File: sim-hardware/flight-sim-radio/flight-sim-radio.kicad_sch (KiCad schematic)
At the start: 22 parts, among them J1 Conn_01x04, J2 Conn_01x03, J3 Conn_01x08, SW1 SW_Push, SW2 SW_Rotary_1x7_MP, SW3 RotaryEncoder_Switch, SW4 RotaryEncoder_Switch, U1 74LS148, U4 TM1637, U5 TM1637

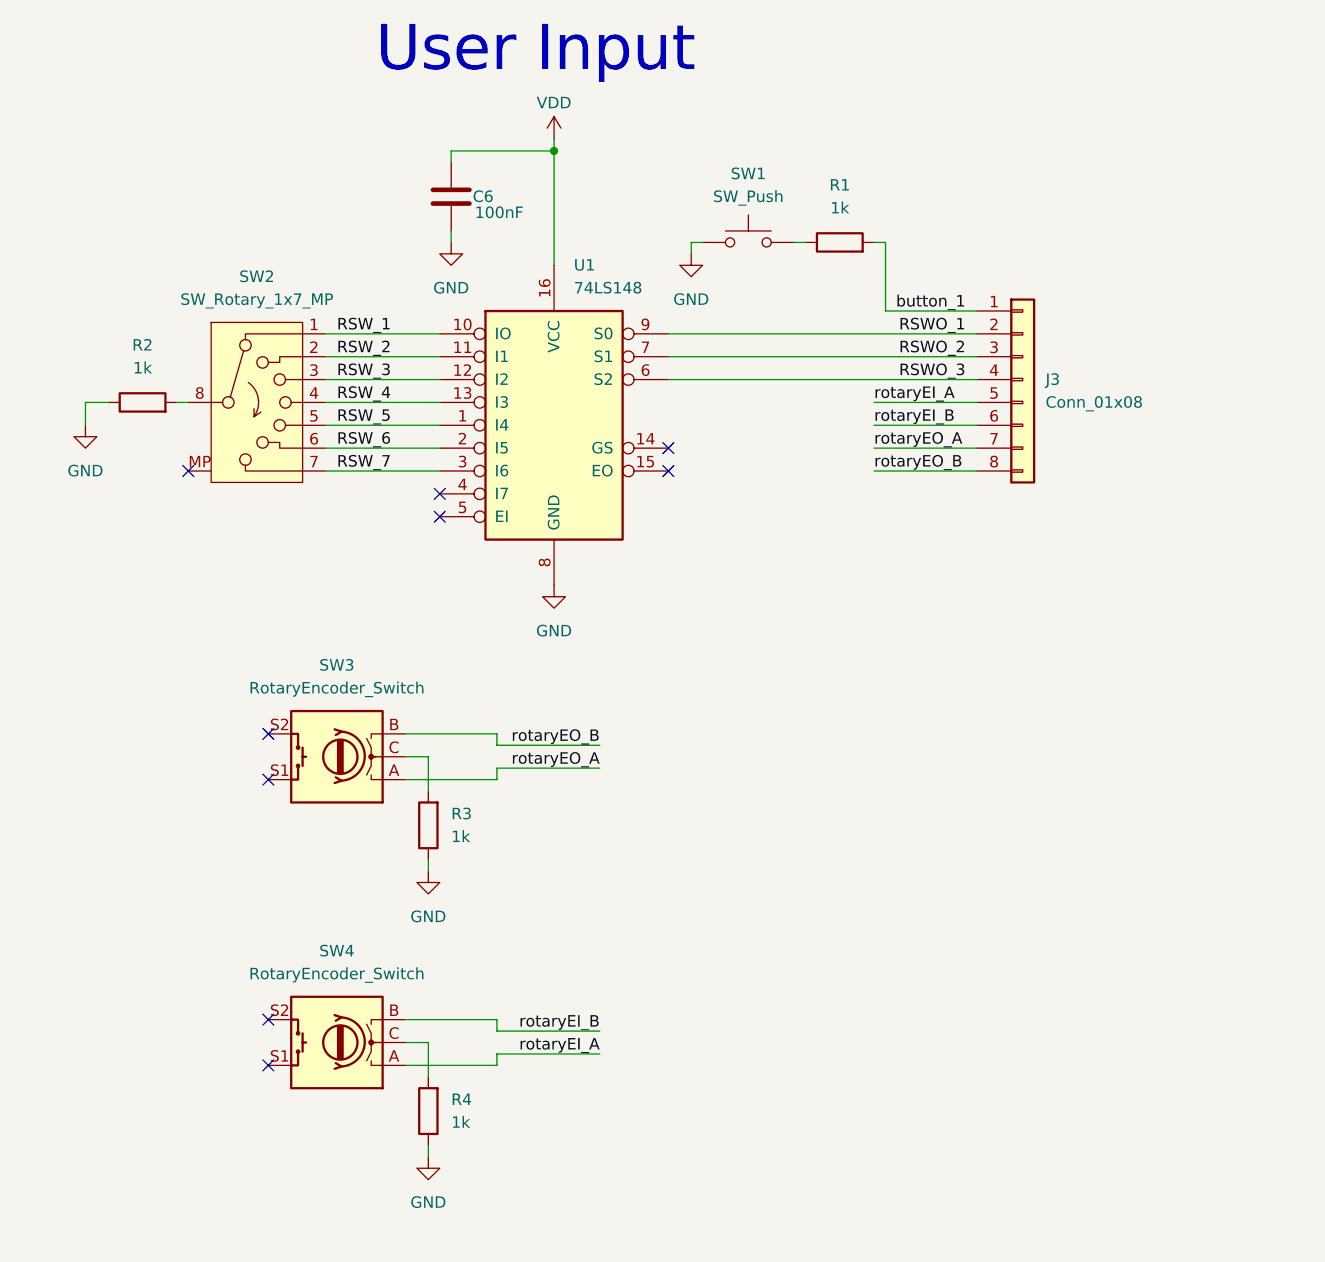
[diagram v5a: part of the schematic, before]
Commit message: input layed out
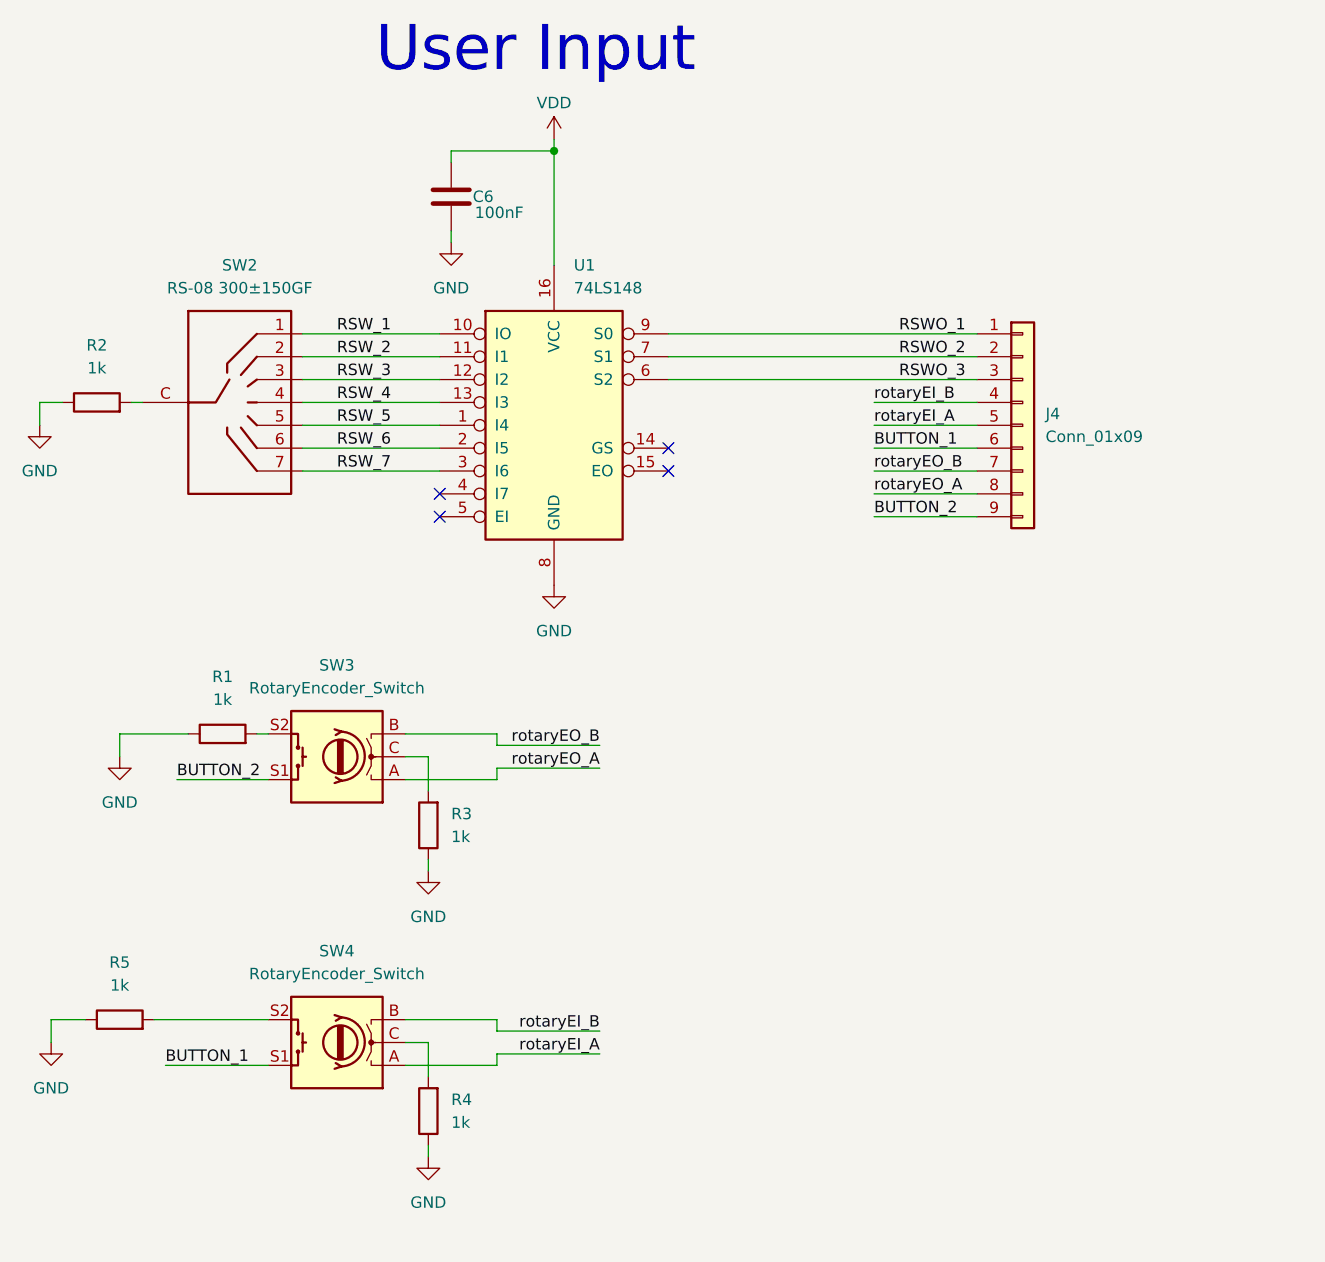
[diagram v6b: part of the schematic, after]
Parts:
- removed J3: Conn_01x08, Connector_PinHeader_2.54mm:PinHeader_1x08_P2.54mm_Vertical, symbol Connector_Generic:Conn_01x08
- removed SW1: SW_Push, Button_Switch_THT:SW_PUSH-12mm, symbol Switch:SW_Push
- removed SW2: SW_Rotary_1x7_MP, Connector_PinHeader_2.54mm:PinHeader_1x09_P2.54mm_Vertical, symbol Switch:SW_Rotary_1x7_MP
- added J4: Conn_01x09, Connector_PinHeader_2.54mm:PinHeader_1x09_P2.54mm_Vertical, symbol Connector_Generic:Conn_01x09
- added R5: 1k, Resistor_THT:R_Axial_DIN0414_L11.9mm_D4.5mm_P15.24mm_Horizontal, symbol Device:R
- added SW2: RS-08 300±150GF, radio_footprints:SW-TH_RS-08-300-150GF, symbol Radio_Components:RS-08 300±150GF
- C1, C4, C5: footprint Capacitor_THT:CP_Axial_L10.0mm_D4.5mm_P15.00mm_Horizontal -> Capacitor_THT:CP_Radial_D8.0mm_P2.50mm
- C2: footprint Capacitor_THT:CP_Axial_L10.0mm_D4.5mm_P15.00mm_Horizontal -> Capacitor_THT:C_Radial_D4.0mm_H5.0mm_P1.50mm
- C3, C6: footprint Capacitor_THT:C_Axial_L3.8mm_D2.6mm_P7.50mm_Horizontal -> Capacitor_THT:C_Radial_D4.0mm_H5.0mm_P1.50mm
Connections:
- net button_1 is gone; now on an unnamed net: R1.2
- net GND: now also R1.1, R5.1
- net RSWO_1: now also J4.1 (Pin_1)
- net RSWO_2: now also J4.2 (Pin_2)
- net RSWO_3: now also J4.3 (Pin_3)
- net RSW_1: now also SW2.1
- net RSW_2: now also SW2.2
- net RSW_3: now also SW2.3
- net RSW_4: now also SW2.4
- net RSW_5: now also SW2.5
- net RSW_6: now also SW2.6
- net RSW_7: now also SW2.7
- net rotaryEI_A: now also J4.5 (Pin_5)
- net rotaryEI_B: now also J4.4 (Pin_4)
- net rotaryEO_A: now also J4.8 (Pin_8)
- net rotaryEO_B: now also J4.7 (Pin_7)
- net at R2.2: now also SW2.C
- net BUTTON_1: now reaches SW4.S1
- net BUTTON_1: now also J4.6 (Pin_6)
- net at SW4.S2: now also R5.2
- net BUTTON_2: now reaches SW3.S1
- net BUTTON_2: now also J4.9 (Pin_9)
- no-connect marks 13 -> 8
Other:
- moved on the sheet: R2

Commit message: PCB routing done
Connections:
- net D1_CLK: now also J1.2 (Pin_2); no longer J1.1 (Pin_1)
- net D1_DIO: now also J1.1 (Pin_1); no longer J1.2 (Pin_2)
- net D2_CLK: now also J1.4 (Pin_4); no longer J1.3 (Pin_3)
- net D2_DIO: now also J1.3 (Pin_3); no longer J1.4 (Pin_4)

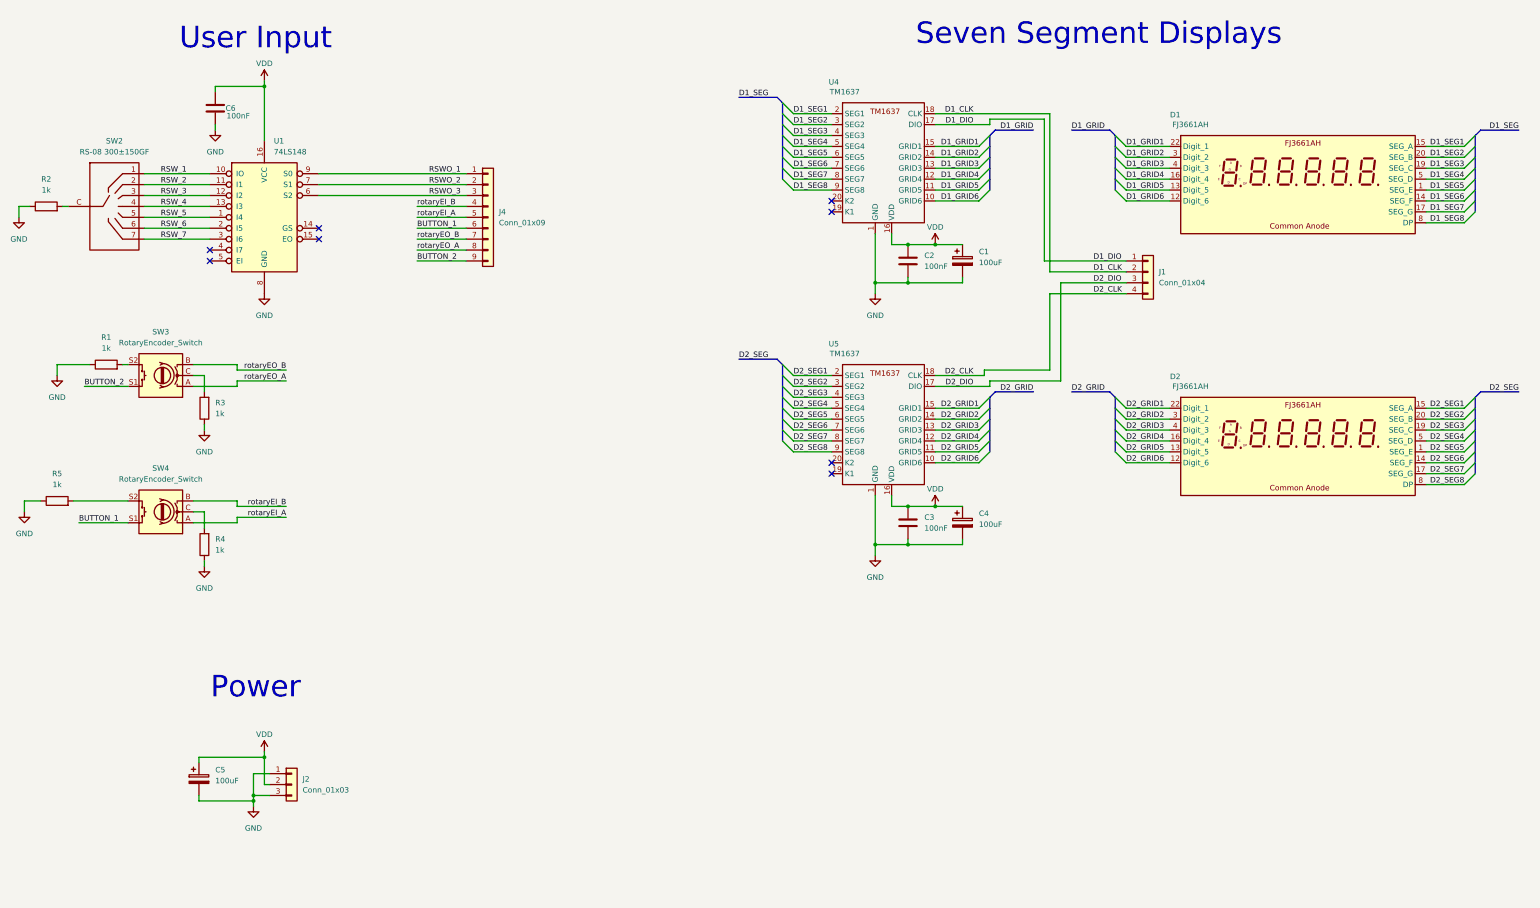
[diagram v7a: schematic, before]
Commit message: PCB routing updated
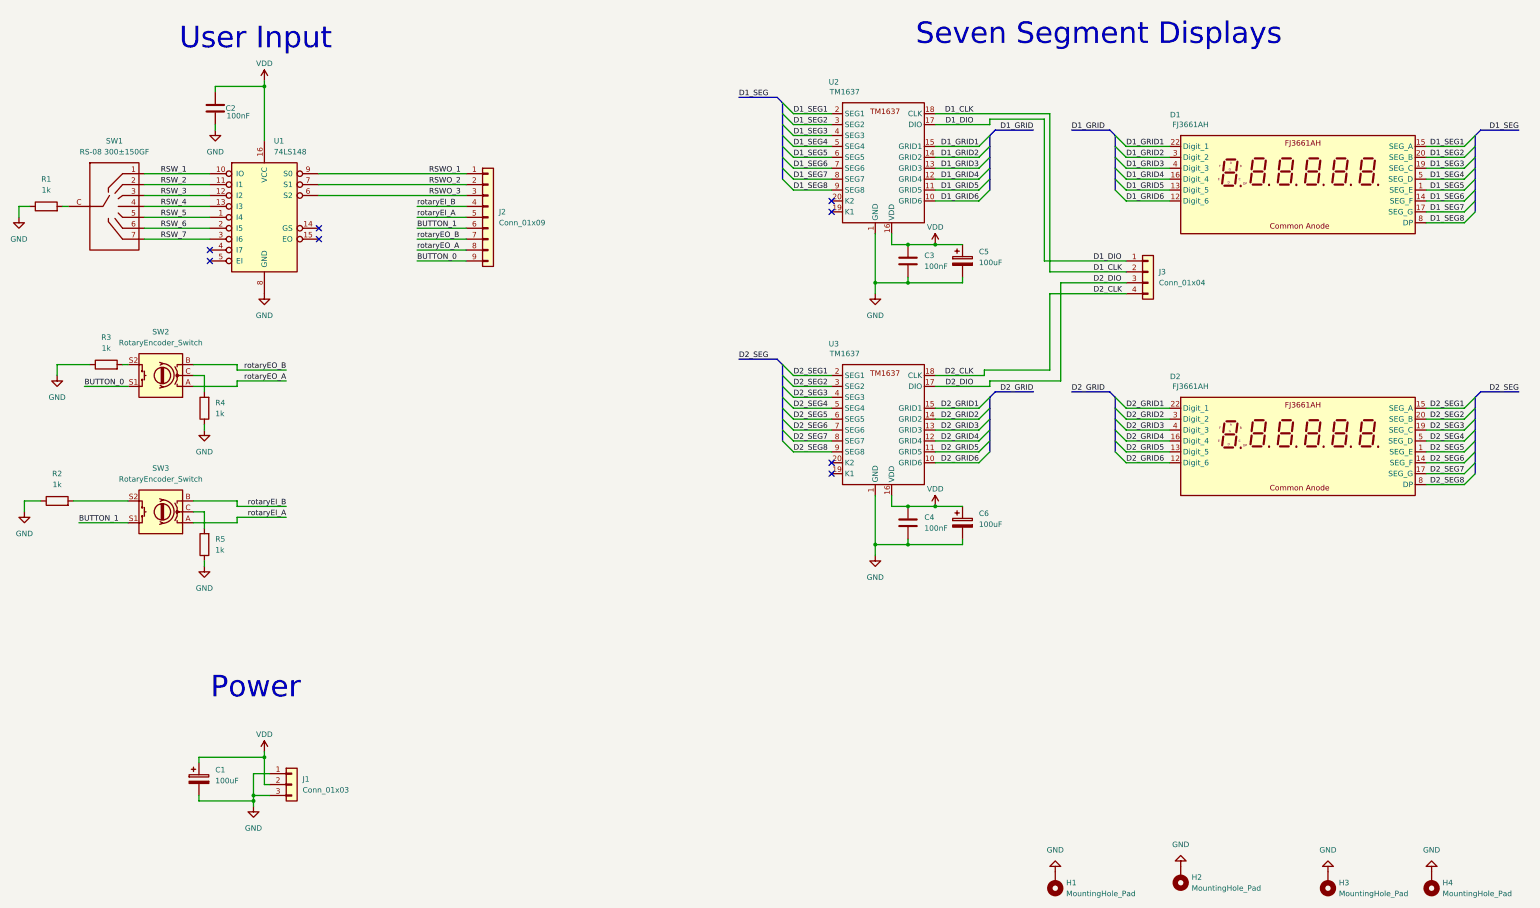
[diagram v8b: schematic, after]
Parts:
- added H1, H2, H3, H4: MountingHole_Pad, MountingHole:MountingHole_2.7mm_M2.5_Pad, symbol Mechanical:MountingHole_Pad
- C1: renamed from C5; footprint Capacitor_THT:CP_Radial_D8.0mm_P2.50mm -> Capacitor_THT:CP_Radial_D4.0mm_P2.00mm
- C2: renamed from C6; footprint Capacitor_THT:C_Radial_D4.0mm_H5.0mm_P1.50mm -> Capacitor_THT:C_Disc_D5.0mm_W2.5mm_P2.50mm
- C3: renamed from C2; footprint Capacitor_THT:C_Radial_D4.0mm_H5.0mm_P1.50mm -> Capacitor_THT:C_Disc_D5.0mm_W2.5mm_P2.50mm
- C4: renamed from C3; footprint Capacitor_THT:C_Radial_D4.0mm_H5.0mm_P1.50mm -> Capacitor_THT:C_Disc_D5.0mm_W2.5mm_P2.50mm
- C5: renamed from C1; footprint Capacitor_THT:CP_Radial_D8.0mm_P2.50mm -> Capacitor_THT:CP_Radial_D4.0mm_P2.00mm
- C6: renamed from C4; footprint Capacitor_THT:CP_Radial_D8.0mm_P2.50mm -> Capacitor_THT:CP_Radial_D4.0mm_P2.00mm
- R1: renamed from R2; footprint Resistor_THT:R_Axial_DIN0414_L11.9mm_D4.5mm_P15.24mm_Horizontal -> Resistor_THT:R_Axial_DIN0207_L6.3mm_D2.5mm_P10.16mm_Horizontal
- R2: renamed from R5; footprint Resistor_THT:R_Axial_DIN0414_L11.9mm_D4.5mm_P15.24mm_Horizontal -> Resistor_THT:R_Axial_DIN0207_L6.3mm_D2.5mm_P10.16mm_Horizontal
- R3: renamed from R1; footprint Resistor_THT:R_Axial_DIN0414_L11.9mm_D4.5mm_P15.24mm_Horizontal -> Resistor_THT:R_Axial_DIN0207_L6.3mm_D2.5mm_P10.16mm_Horizontal
- R4: renamed from R3; footprint Resistor_THT:R_Axial_DIN0414_L11.9mm_D4.5mm_P15.24mm_Horizontal -> Resistor_THT:R_Axial_DIN0207_L6.3mm_D2.5mm_P10.16mm_Horizontal
- R5: renamed from R4; footprint Resistor_THT:R_Axial_DIN0414_L11.9mm_D4.5mm_P15.24mm_Horizontal -> Resistor_THT:R_Axial_DIN0207_L6.3mm_D2.5mm_P10.16mm_Horizontal
- SW2: renamed from SW3; footprint Rotary_Encoder:RotaryEncoder_Alps_EC11E-Switch_Vertical_H20mm_CircularMountingHoles -> radio_footprints:ALPSALPINE EC11E09444A8
- SW3: renamed from SW4; footprint Rotary_Encoder:RotaryEncoder_Alps_EC11E-Switch_Vertical_H20mm_CircularMountingHoles -> radio_footprints:ALPSALPINE EC11E09444A8
- renumbered J2 to J1, J4 to J2, J1 to J3, SW2 to SW1, U4 to U2, U5 to U3
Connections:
- net GND: now also H1.1, H2.1, H3.1, H4.1
- net BUTTON_2 renamed BUTTON_0
